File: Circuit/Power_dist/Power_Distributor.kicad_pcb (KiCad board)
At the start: 2 copper layers, 135.1 x 108.9 mm, 97 parts, among them CON1 Conn-PCIE-x16, J1 Thruster_Off_Switch, P1 XT60, P11 XT60, P15 USB_B, P16 XT60, P17 XT60, P2 XT30, P3 XT30, P4 XT30, P5 XT30, Q1 IPD90P03P4L, Q2 IPD90P03P4L, Q3 IPD90P03P4L, Q5 IPD90P03P4L, Q6 AUIRFS8409-7P, Q7 AUIRFS8409-7P, U1 93LC56BT-I/OT, U2 FT232H, U3 ACPL-247-500E, U4 ACPL-247-500E, U5 LTC4357, U6 LTC4357, U7 UWE-12/6-Q12P, U8 TEN_20-2411WIN, Y1 12MHz

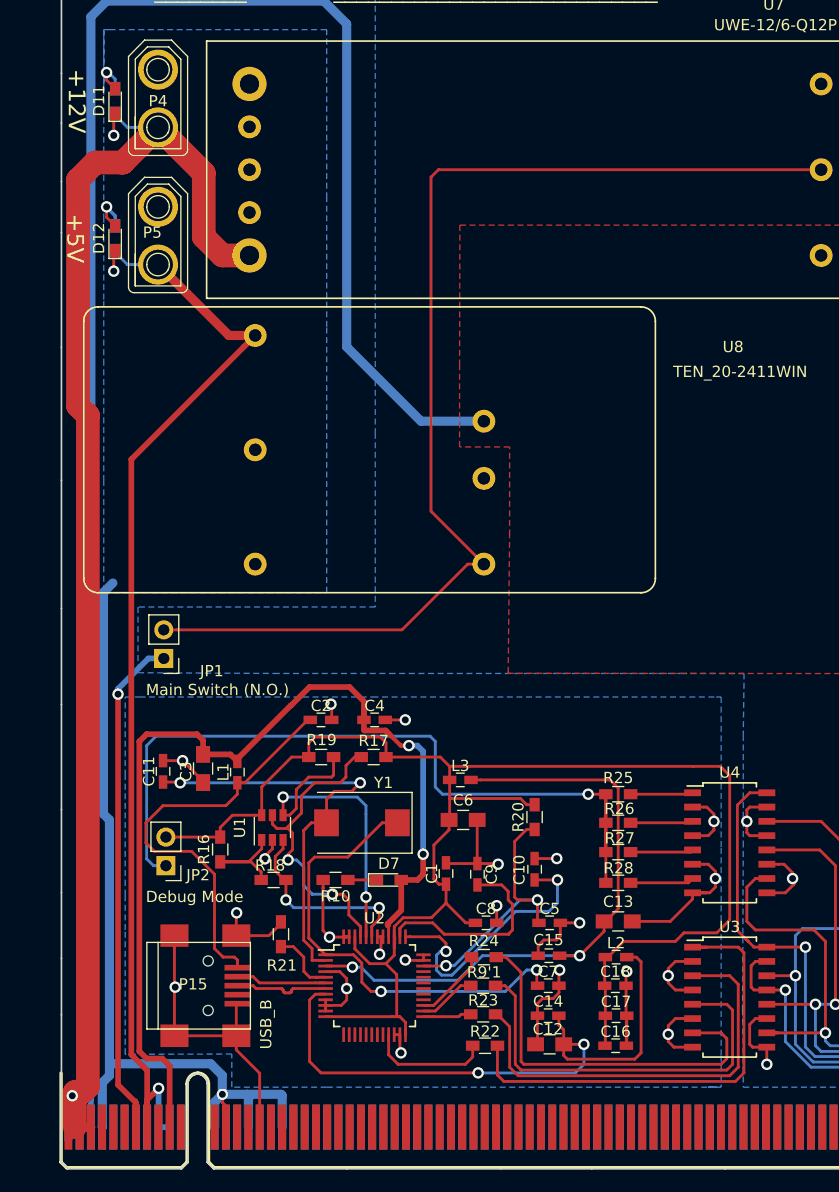
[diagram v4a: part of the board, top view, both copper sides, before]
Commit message: fix USB_B Conn too far from edge
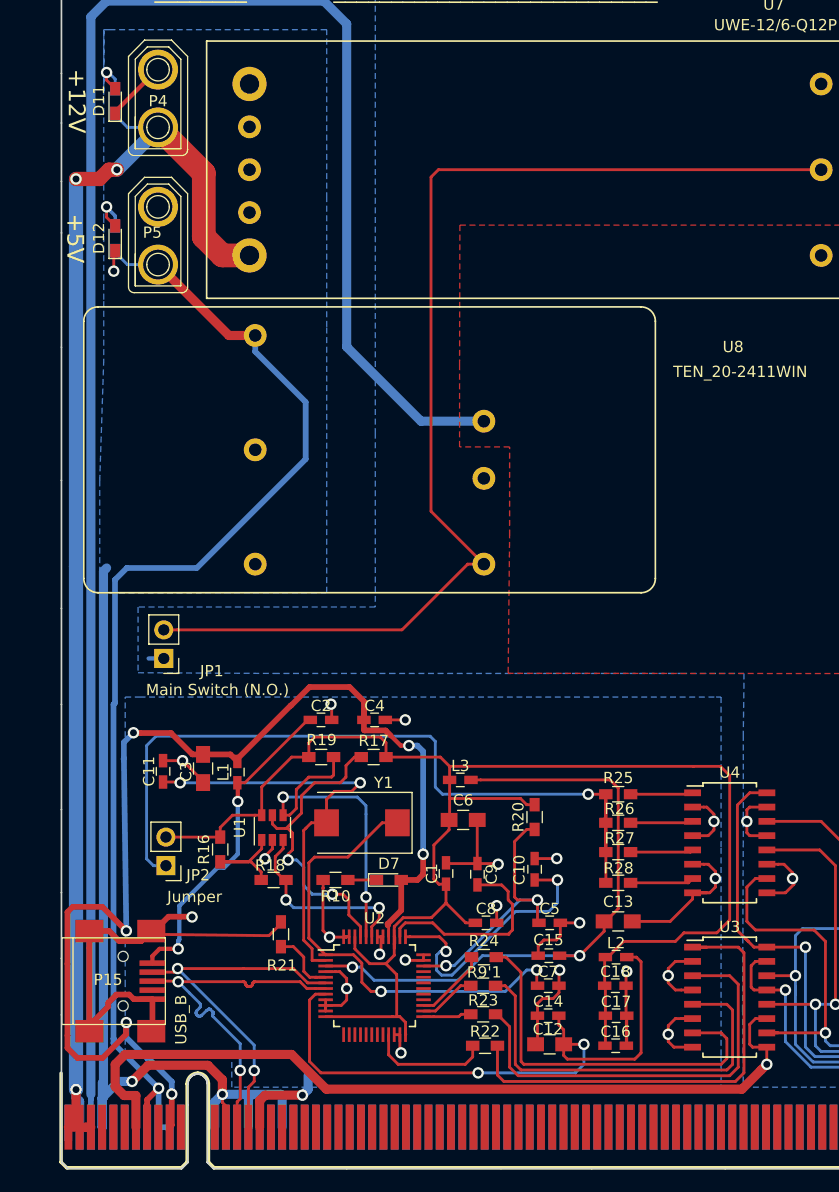
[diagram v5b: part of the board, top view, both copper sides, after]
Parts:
- JP2: value Debug Mode -> Jumper
- moved P15 7.57 mm to (56.1, 125.2)
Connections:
- CON1 pad B14: /D+ -> D+
- CON1 pad B15: /D- -> D-
- P15 pad 2: /Power_Controller/D- -> D-
- P15 pad 3: /Power_Controller/D+ -> D+
- U2 pad 6: /Power_Controller/D- -> D-
- U2 pad 7: /Power_Controller/D+ -> D+
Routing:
- net D+: track 0.00 -> 33.3 mm, vias 0 -> 2
- net GNDREF: track 107.5 -> 140.7 mm
- net D-: track 0.00 -> 33.2 mm, vias 0 -> 2
- net GND: track 98.6 -> 118.8 mm, vias 8 -> 7
- net VBUS: track 90.0 -> 108.7 mm, vias 2 -> 6
- net GNDD: track 132.3 -> 150.7 mm
- net /Power_Controller/D-: track 8.97 -> 0.00 mm
- net Net-(C2-Pad1): track 37.8 -> 29.3 mm, vias 0 -> 2
- net /Power_Controller/D+: track 8.38 -> 0.00 mm
- net +5V: track 101.5 -> 107.3 mm
- net +12V: track 124.2 -> 123.4 mm, vias 1 -> 3
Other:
- net class Default: clearance 0.2032 -> 0.1524
- rule trace_clearance: 0.2032 -> 0.1524
